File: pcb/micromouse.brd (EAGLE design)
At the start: 71.1 x 48.3 mm, 33 parts, among them J1 ENCODER_POLOLU, J2 ENCODER_POLOLU, Q1 PFET, U1 DRV8833PWP, U2 LD1117

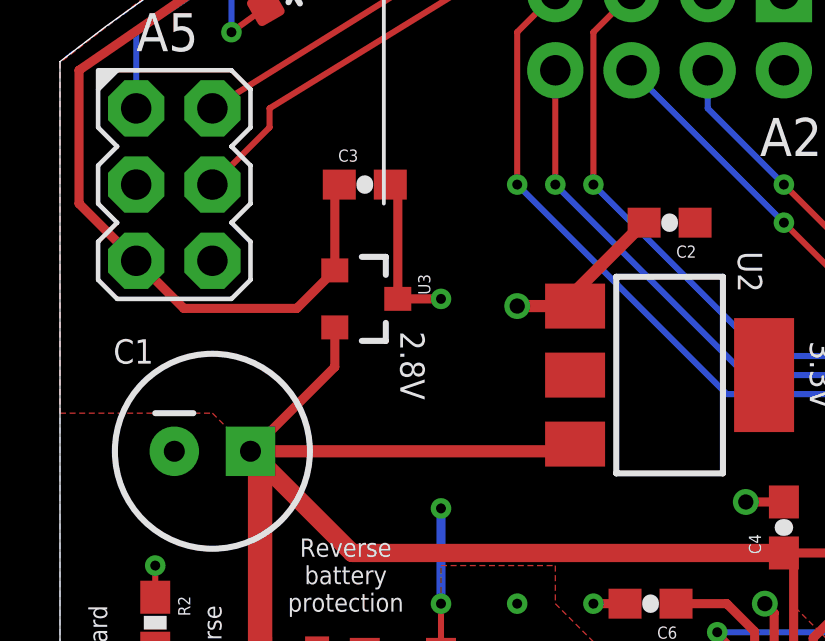
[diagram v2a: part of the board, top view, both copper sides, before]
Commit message: Fixed 2.8v regulator pinout
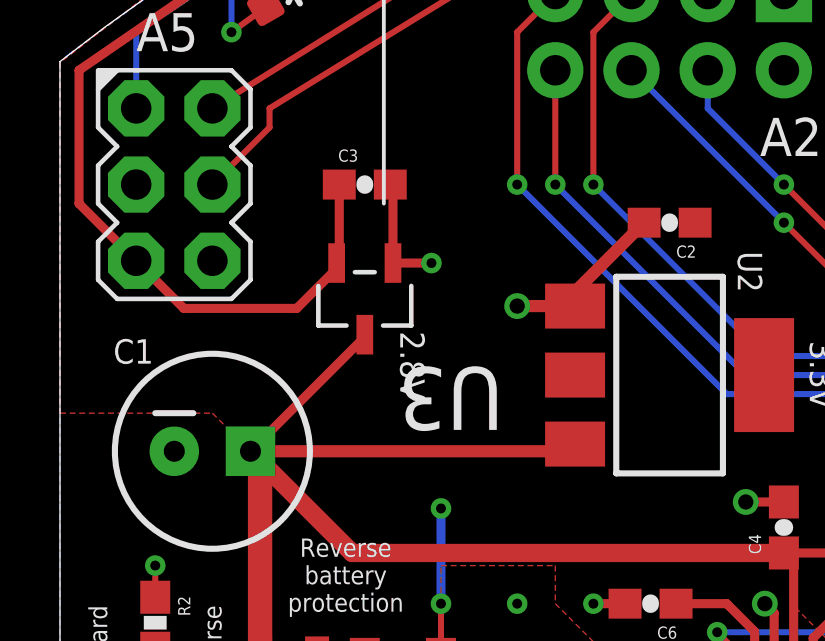
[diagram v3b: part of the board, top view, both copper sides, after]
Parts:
- R2: value 2K -> 1K
- R6, R7: value 681 -> 332
- U3: value (none) -> MCP1703T-2802E/CB; device SparkFun-PowerIC:SOT23-3 -> Microchip_By_element14_Batch_1:SOT95P300X145-3N
- turned U3 to 180 degrees
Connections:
- net 2.8V: now also U3.2; no longer U3.1
- net GND: now also U3.1; no longer U3.3
- net VDD: now also U3.3; no longer U3.2
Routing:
- net GND: track 26.7 -> 25.4 mm
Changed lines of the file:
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@@
 </element>
 <element name="R1" library="SparkFun-Resistors" package="0603-RES" value="100K" x="10.16" y="15.24" rot="R270"/>
-<element name="R2" library="SparkFun-Resistors" package="0603-RES" value="2K" x="3.175" y="17.145" rot="R270"/>
+<element name="R2" library="SparkFun-Resistors" package="0603-RES" value="1K" x="3.175" y="17.145" rot="R270"/>
 <element name="R3" library="SparkFun-Resistors" package="0603-RES" value="3.3k" x="27.94" y="44.45" rot="R270"/>
 <element name="R4" library="SparkFun-Resistors" package="0603-RES" value="3.3k" x="25.4" y="44.45" rot="R90"/>
 <element name="R5" library="SparkFun-Resistors" package="0603-RES" value="33k" x="12.7" y="15.24" rot="R270"/>
-<element name="R6" library="SparkFun-Resistors" package="0603-RES" value="681" x="60.325" y="40.005" rot="R150"/>
-<element name="R7" library="SparkFun-Resistors" package="0603-RES" value="681" x="10.795" y="40.005" rot="R210"/>
+<element name="R6" library="SparkFun-Resistors" package="0603-RES" value="332" x="60.325" y="40.005" rot="R150"/>
+<element name="R7" library="SparkFun-Resistors" package="0603-RES" value="332" x="10.795" y="40.005" rot="R210"/>
 <element name="U1" library="Custom" package="HTSSOP-16" value="DRV8833PWP" x="24.13" y="12.7" smashed="yes">
 <attribute name="NAME" x="21.2344" y="10.6172" size="1.016" layer="25" ratio="10" rot="R90"/>
@@
 <attribute name="NAME" x="22.5933" y="29.5275" size="0.8128" layer="25" rot="SR270"/>
 </element>
-<element name="U3" library="SparkFun-PowerIC" package="SOT23-3" value="" x="10.16" y="27.94" rot="R270"/>
 <element name="C4" library="SparkFun-Capacitors" package="0603-CAP" value="1uF" x="24.13" y="20.32" rot="R90"/>
 <element name="BZ1" library="Custom" package="BUZZER" value="BUZZER" x="49.53" y="36.5125" smashed="yes" rot="R135">
@@
 <element name="R8" library="SparkFun-Resistors" package="0603-RES" value="100K" x="54.9275" y="27.305" rot="R270"/>
 <element name="R9" library="SparkFun-Resistors" package="0603-RES" value="132" x="53.0225" y="27.305" rot="R90"/>
+<element name="U3" library="Microchip_By_element14_Batch_1" package="SOT95P300X145-3N" value="MCP1703T-2802E/CB" x="10.16" y="27.94" rot="R180">
+<attribute name="PACKAGE" value="SOT-3" x="10.16" y="27.94" size="1.778" layer="27" rot="R180" display="off"/>
+<attribute name="OC_NEWARK" value="40M0634" x="10.16" y="27.94" size="1.778" layer="27" rot="R180" display="off"/>
+<attribute name="MPN" value="MCP1703T-3002E/CB" x="10.16" y="27.94" size="1.778" layer="27" rot="R180" display="off"/>
+<attribute name="SUPPLIER" value="Microchip" x="10.16" y="27.94" size="1.778" layer="27" rot="R180" display="off"/>
+<attribute name="OC_FARNELL" value="1439517" x="10.16" y="27.94" size="1.778" layer="27" rot="R180" display="off"/>
+</element>
 </elements>
 <signals>
@@
 <contactref element="U2" pad="1"/>
 <contactref element="C2" pad="2"/>
-<contactref element="U3" pad="3"/>
 <contactref element="C3" pad="2"/>
 <contactref element="R2" pad="1"/>
@@
 <via x="26.035" y="11.43" extent="1-16" drill="0.3302"/>
 <via x="22.225" y="11.43" extent="1-16" drill="0.3302"/>
-<wire x1="11.26" y1="27.94" x2="11.26" y2="31.5" width="0.3048" layer="1"/>
 <wire x1="11.26" y1="31.5" x2="11.01" y2="31.75" width="0.4064" layer="1"/>
-<wire x1="11.26" y1="27.94" x2="12.7" y2="27.94" width="0.3048" layer="1"/>
-<via x="12.7" y="27.94" extent="1-16" drill="0.3302"/>
 <wire x1="59.588878125" y1="40.429996875" x2="58.1025" y2="41.275" width="0.2032" layer="1"/>
 <via x="58.1025" y="41.275" extent="1-16" drill="0.3302"/>
@@
 <via x="56.1975" y="29.7975" extent="1-16" drill="0.508"/>
 <via x="56.1975" y="26.455" extent="1-16" drill="0.3302"/>
+<contactref element="U3" pad="1"/>
+<wire x1="11.26" y1="31.5" x2="11.0998" y2="31.3398" width="0.3048" layer="1"/>
+<wire x1="11.0998" y1="31.3398" x2="11.0998" y2="29.1338" width="0.3048" layer="1"/>
+<wire x1="11.0998" y1="29.1338" x2="12.3825" y2="29.1338" width="0.3048" layer="1"/>
+<via x="12.3825" y="29.1338" extent="1-16" drill="0.3302"/>
 </signal>
 <signal name="VDD">
@@
 <contactref element="C1" pad="1"/>
 <contactref element="U2" pad="3"/>
-<contactref element="U3" pad="2"/>
 <contactref element="C5" pad="1"/>
 <contactref element="U1" pad="12"/>
@@
 <wire x1="17.17" y1="23.1" x2="16.93" y2="22.86" width="0.4064" layer="1"/>
 <wire x1="16.93" y1="22.86" x2="6.35" y2="22.86" width="0.4064" layer="1"/>
-<wire x1="9.16" y1="26.99" x2="9.16" y2="25.67" width="0.3048" layer="1"/>
-<wire x1="9.16" y1="25.67" x2="6.35" y2="22.86" width="0.3048" layer="1"/>
+<wire x1="10.16" y1="26.67" x2="6.35" y2="22.86" width="0.3048" layer="1"/>
 <wire x1="24.13" y1="19.47" x2="26.24" y2="19.47" width="0.3048" layer="1"/>
 <wire x1="26.24" y1="19.47" x2="26.67" y2="19.9" width="0.3048" layer="1"/>
+<contactref element="U3" pad="3"/>
+<wire x1="10.16" y1="26.7462" x2="10.16" y2="26.67" width="0.3048" layer="1"/>
 </signal>
 <signal name="3.3V">
@@
 </signal>
 <signal name="2.8V">
-<contactref element="U3" pad="1"/>
 <contactref element="C3" pad="1"/>
 <contactref element="R3" pad="1"/>
@@
 <wire x1="33.02" y1="45.72" x2="33.02" y2="47.481703125" width="0.3048" layer="1"/>
 <wire x1="33.02" y1="47.481703125" x2="32.984878125" y2="47.516825" width="0.3048" layer="1"/>
-<wire x1="9.16" y1="28.89" x2="9.16" y2="31.6" width="0.3048" layer="1"/>
 <wire x1="9.16" y1="31.6" x2="9.31" y2="31.75" width="0.4064" layer="1"/>
-<wire x1="9.16" y1="28.89" x2="7.8925" y2="27.6225" width="0.3048" layer="1"/>
 <wire x1="7.8925" y1="27.6225" x2="4.1275" y2="27.6225" width="0.3048" layer="1"/>
 <wire x1="4.1275" y1="27.6225" x2="2.54" y2="29.21" width="0.3048" layer="1"/>
@@
 <wire x1="25.4" y1="46.579115625" x2="25.47470625" y2="46.653821875" width="0.2032" layer="1"/>
 <wire x1="27.94" y1="45.3" x2="27.94" y2="47.082928125" width="0.2032" layer="1"/>
+<contactref element="U3" pad="2"/>
+<wire x1="7.8925" y1="27.6225" x2="9.2202" y2="28.9502" width="0.3048" layer="1"/>
+<wire x1="9.2202" y1="28.9502" x2="9.2202" y2="29.1338" width="0.3048" layer="1"/>
+<wire x1="9.2202" y1="28.9502" x2="9.31" y2="29.04" width="0.3048" layer="1"/>
+<wire x1="9.31" y1="29.04" x2="9.31" y2="31.75" width="0.3048" layer="1"/>
 </signal>
 <signal name="SCL">

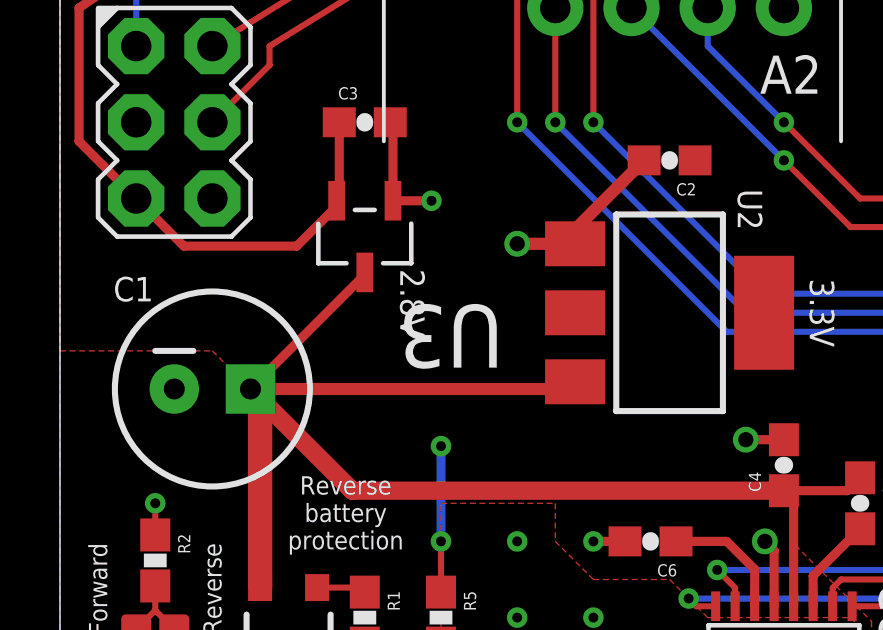
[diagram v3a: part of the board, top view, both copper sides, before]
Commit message: Changed led resistors
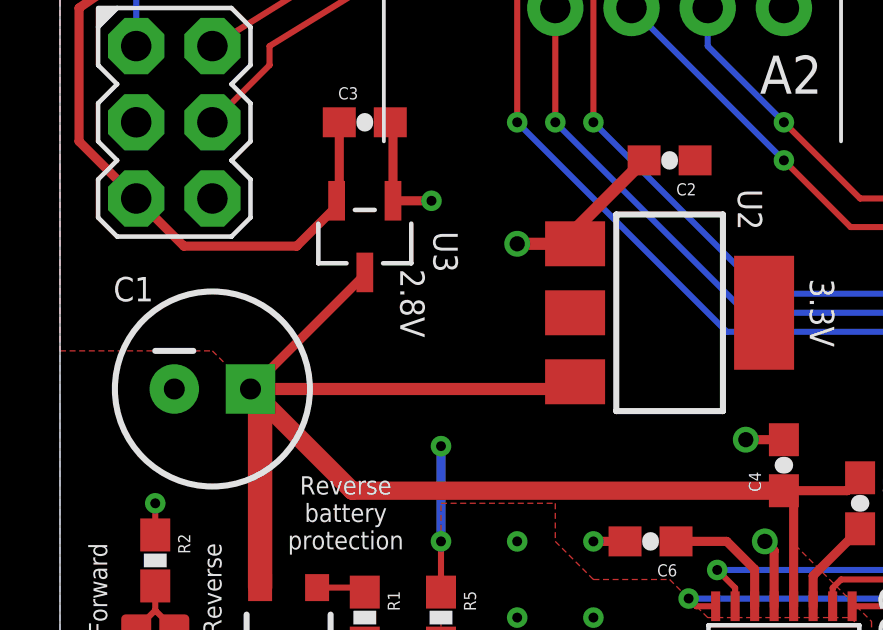
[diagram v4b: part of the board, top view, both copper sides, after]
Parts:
- R6, R7: value 332 -> 100
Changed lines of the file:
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@@
 <element name="R4" library="SparkFun-Resistors" package="0603-RES" value="3.3k" x="25.4" y="44.45" rot="R90"/>
 <element name="R5" library="SparkFun-Resistors" package="0603-RES" value="33k" x="12.7" y="15.24" rot="R270"/>
-<element name="R6" library="SparkFun-Resistors" package="0603-RES" value="332" x="60.325" y="40.005" rot="R150"/>
-<element name="R7" library="SparkFun-Resistors" package="0603-RES" value="332" x="10.795" y="40.005" rot="R210"/>
+<element name="R6" library="SparkFun-Resistors" package="0603-RES" value="100" x="60.325" y="40.005" rot="R150"/>
+<element name="R7" library="SparkFun-Resistors" package="0603-RES" value="100" x="10.795" y="40.005" rot="R210"/>
 <element name="U1" library="Custom" package="HTSSOP-16" value="DRV8833PWP" x="24.13" y="12.7" smashed="yes">
 <attribute name="NAME" x="21.2344" y="10.6172" size="1.016" layer="25" ratio="10" rot="R90"/>
@@
 <element name="R8" library="SparkFun-Resistors" package="0603-RES" value="100K" x="54.9275" y="27.305" rot="R270"/>
 <element name="R9" library="SparkFun-Resistors" package="0603-RES" value="132" x="53.0225" y="27.305" rot="R90"/>
-<element name="U3" library="Microchip_By_element14_Batch_1" package="SOT95P300X145-3N" value="MCP1703T-2802E/CB" x="10.16" y="27.94" rot="R180">
+<element name="U3" library="Microchip_By_element14_Batch_1" package="SOT95P300X145-3N" value="MCP1703T-2802E/CB" x="10.16" y="27.94" smashed="yes" rot="R180">
 <attribute name="PACKAGE" value="SOT-3" x="10.16" y="27.94" size="1.778" layer="27" rot="R180" display="off"/>
 <attribute name="OC_NEWARK" value="40M0634" x="10.16" y="27.94" size="1.778" layer="27" rot="R180" display="off"/>
@@
 <attribute name="SUPPLIER" value="Microchip" x="10.16" y="27.94" size="1.778" layer="27" rot="R180" display="off"/>
 <attribute name="OC_FARNELL" value="1439517" x="10.16" y="27.94" size="1.778" layer="27" rot="R180" display="off"/>
+<attribute name="NAME" x="12.446" y="28.1178" size="0.8128" layer="25" ratio="10" rot="SR270"/>
 </element>
 </elements>

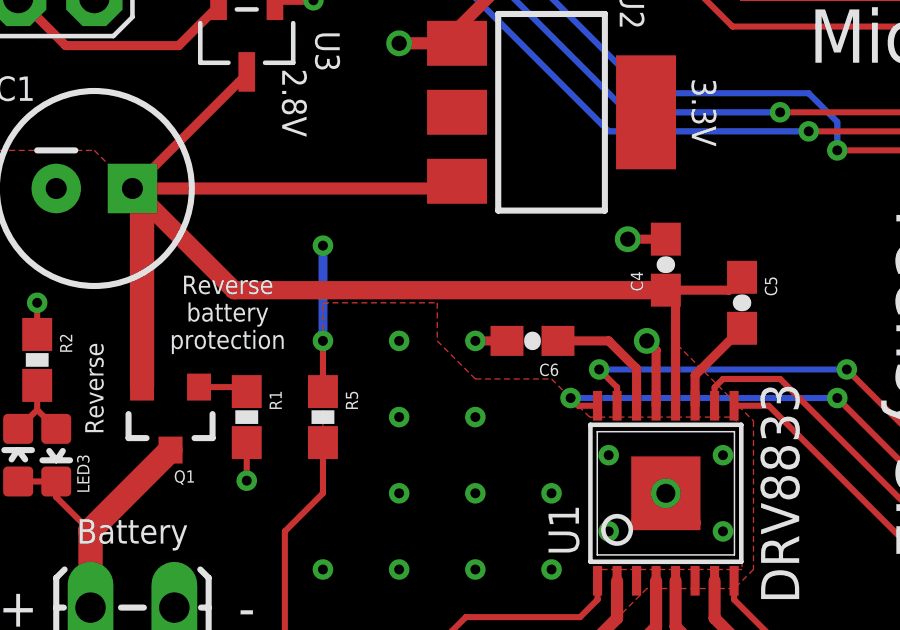
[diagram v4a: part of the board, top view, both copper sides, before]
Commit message: Fixed nsleep signal on board
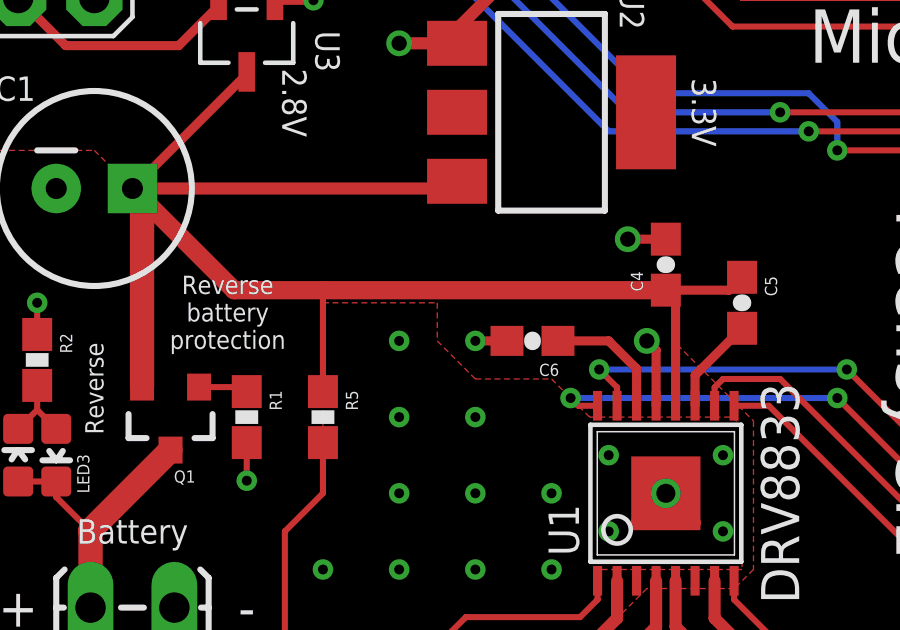
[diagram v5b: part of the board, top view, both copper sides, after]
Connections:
- net 3.3V: no longer R5.1
- net VDD: now also R5.1
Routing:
- net 3.3V: track 4.86 -> 0.00 mm, vias 2 -> 0
- net VDD: track 48.6 -> 52.0 mm
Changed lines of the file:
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@@
 <wire x1="6.67" y1="22.54" x2="6.35" y2="22.86" width="0.8128" layer="1"/>
 <wire x1="6.67" y1="22.54" x2="9.74" y2="19.47" width="0.6096" layer="1"/>
-<wire x1="9.74" y1="19.47" x2="24.13" y2="19.47" width="0.6096" layer="1"/>
+<wire x1="9.74" y1="19.47" x2="12.7" y2="19.47" width="0.6096" layer="1"/>
+<wire x1="12.7" y1="19.47" x2="24.13" y2="19.47" width="0.6096" layer="1"/>
 <wire x1="24.13" y1="19.47" x2="24.455" y2="19.145" width="0.3048" layer="1"/>
 <wire x1="24.455" y1="19.145" x2="24.455" y2="15.6178" width="0.3048" layer="1"/>
@@
 <contactref element="U3" pad="3"/>
 <wire x1="10.16" y1="26.7462" x2="10.16" y2="26.67" width="0.3048" layer="1"/>
+<contactref element="R5" pad="1"/>
+<wire x1="12.7" y1="16.09" x2="12.7" y2="19.47" width="0.2032" layer="1"/>
 </signal>
 <signal name="3.3V">
@@
 <contactref element="J2" pad="3"/>
 <contactref element="J1" pad="3"/>
-<contactref element="R5" pad="1"/>
 <contactref element="A2" pad="2"/>
 <contactref element="A1" pad="3.3V"/>
-<wire x1="12.7" y1="16.09" x2="12.7" y2="17.78" width="0.2032" layer="1"/>
-<via x="12.7" y="17.78" extent="1-16" drill="0.3302"/>
 <polygon width="0.3048" layer="1">
 <vertex x="10.16" y="5.08"/>
@@
 <vertex x="15.24" y="5.08"/>
 </polygon>
-<wire x1="12.7" y1="17.78" x2="12.7" y2="20.955" width="0.3048" layer="16"/>
-<via x="12.7" y="20.955" extent="1-16" drill="0.3302"/>
 <contactref element="BZ1" pad="+"/>
 </signal>
